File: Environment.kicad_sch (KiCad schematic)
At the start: 17 parts, among them J7 TEMP1, U6 EMC2301, U8 DS18B20U

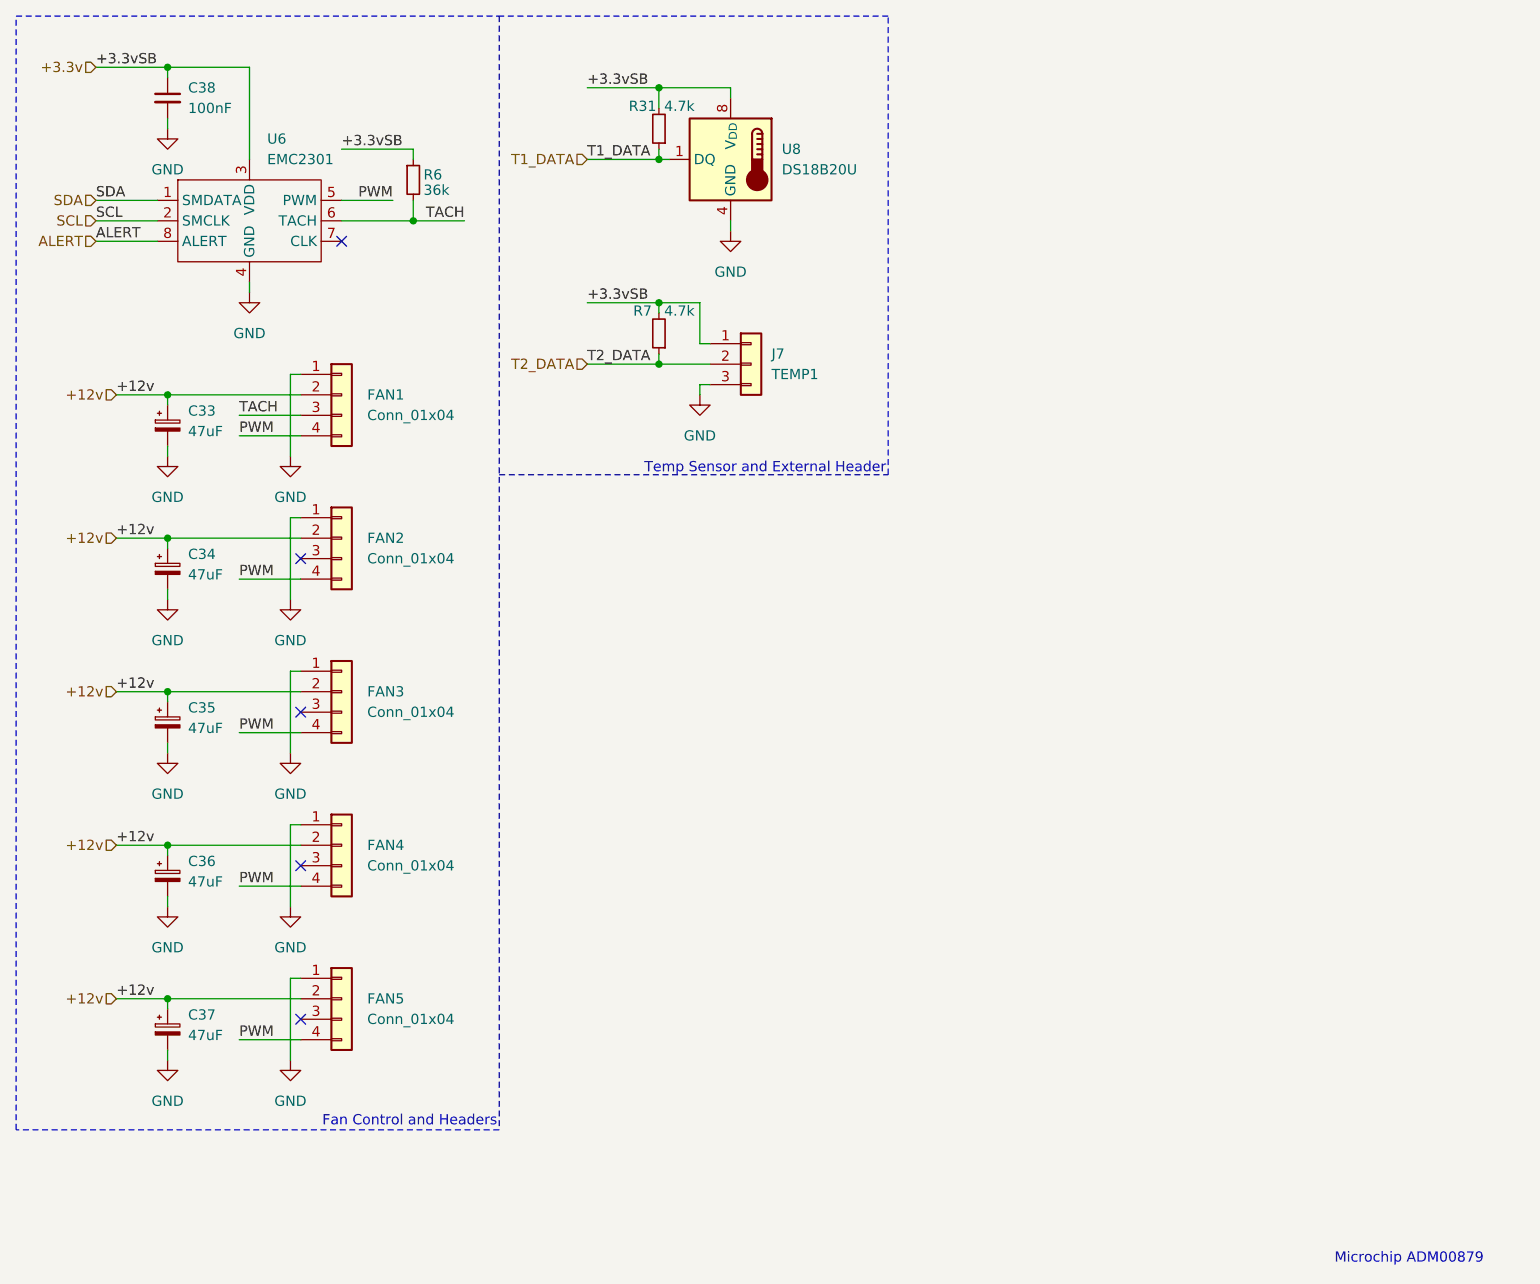
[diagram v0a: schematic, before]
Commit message: rev5
Added MACROM (specific ROM holding MAC address and (optionally) board
revision)
Added more circuitry to protect the EMC2301, allowing for use with fans
with internal pull-ups.
Added USB-C
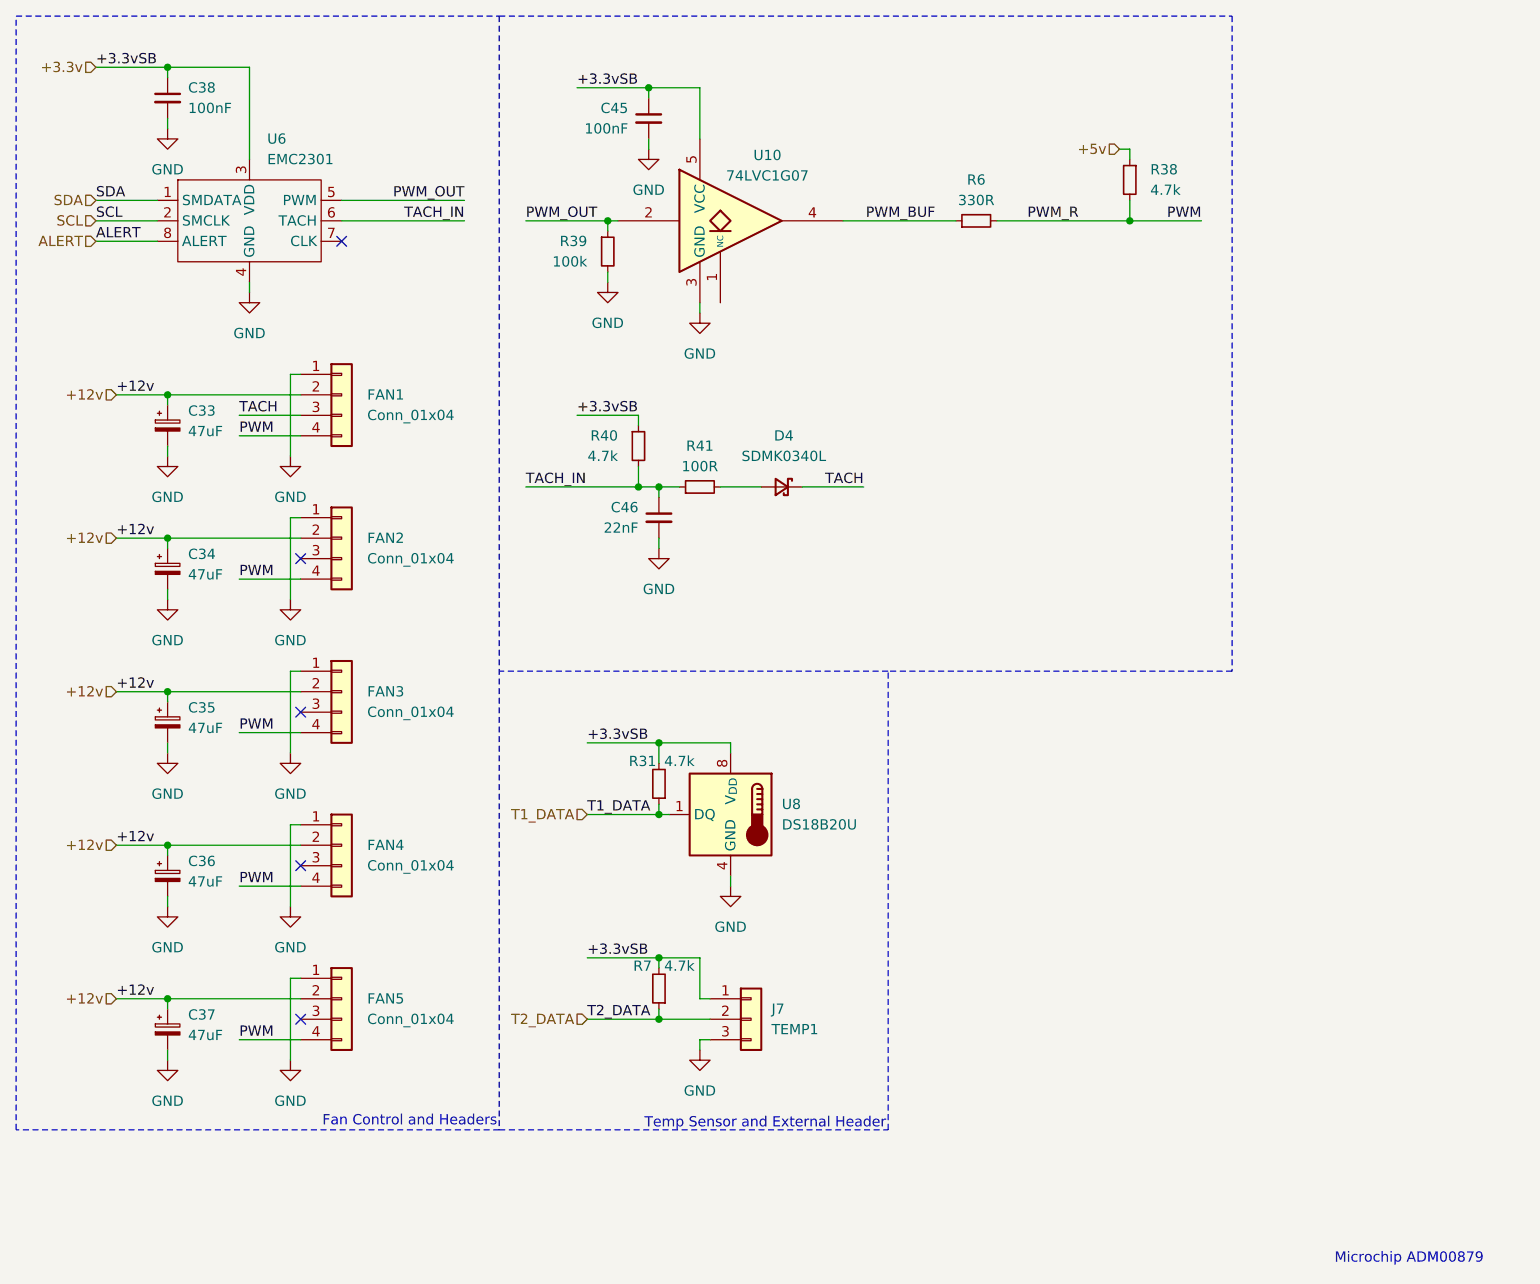
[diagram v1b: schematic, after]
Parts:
- added C45: 100nF, Capacitor_SMD:C_0402_1005Metric, symbol Device:C_Small
- added C46: 22nF, Capacitor_SMD:C_0402_1005Metric, symbol Device:C_Small
- added D4: SDMK0340L, Diode_SMD:D_SOD-323, symbol Device:D_Schottky_Small
- added R38, R40: 4.7k, Resistor_SMD:R_0402_1005Metric, symbol Device:R_Small
- added R39: 100k, Capacitor_SMD:C_0402_1005Metric, symbol Device:R_Small
- added R41: 100R, Capacitor_SMD:C_0402_1005Metric, symbol Device:R_Small
- added U10: 74LVC1G07, Package_TO_SOT_SMD:SOT-23-5, symbol 74xGxx:74LVC1G07
- C33, C34, C35, C36, C37: JLCPCB_PN C2836440 -> (none); LCSC Part # (none) -> C2836440
- C38: JLCPCB_PN C1525 -> (none); LCSC Part # (none) -> C1525
- FAN1, FAN2, FAN3, FAN4, FAN5: JLCPCB_PN C240840 -> (none); LCSC Part # (none) -> C240840
- J7: JLCPCB_PN C49257 -> (none); LCSC Part # (none) -> C2937625
- R31, R7: JLCPCB_PN C25900 -> (none); LCSC Part # (none) -> C25900
- R6: value 36k -> 330R; JLCPCB_PN C25744 -> (none); LCSC Part # (none) -> C25104
- U6: JLCPCB_PN C148036 -> (none); LCSC Part # (none) -> C148036
- U8: JLCPCB_PN C695836 -> (none); LCSC Part # (none) -> C695836
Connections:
- net +3.3v: now also C45.1, R40.1, U10.5 (VCC); no longer R6.1
- net GND: now also C45.2, C46.2, R39.2, U10.3 (GND)
- net PWM: now also R6.2, R38.2; no longer U6.5 (PWM)
- net TACH: now also D4.1 (K); no longer R6.2, U6.6 (TACH)
- new net: D4.2 (A), R41.2
- new net +5v: R38.1
- new net PWM_BUF: R6.1, U10.4
- new net PWM_OUT: R39.1, U10.2, U6.5 (PWM)
- new net TACH_IN: C46.1, R40.2, R41.1, U6.6 (TACH)
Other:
- moved on the sheet: J7, R31, R7, U8
